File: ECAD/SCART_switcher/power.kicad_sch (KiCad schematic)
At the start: 18 parts, among them U12 L7805, U13 L7809, U14 TL431DBZ

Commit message: progressed ecad
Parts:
- removed U14: TL431DBZ, Package_TO_SOT_SMD:SOT-23, symbol Reference_Voltage:TL431DBZ
- added C?: 100nC, Capacitor_SMD:C_0805_2012Metric_Pad1.18x1.45mm_HandSolder, symbol Device:C
- added R? (x4): 10kR, Resistor_SMD:R_0805_2012Metric_Pad1.20x1.40mm_HandSolder, symbol Device:R
- added SW1: SW_Push_DPDT, symbol Switch:SW_Push_DPDT
- added U? (x3): RC4580, symbol Amplifier_Operational:NE5532
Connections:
- net +12V: now also C?.1, U?.8 (V+)
- net +2V5: now also U?.1, U?.2 (-)
- net +4V5: now also U?.6 (-), U?.7
- net +5V: now also R?.1
- net +9V: now also R?.1
- net GND: now also C?.2, R?.2, R?.2, U?.4 (V-)
- net at D?.2 (A2), Q?.5 (D), Q?.6 (D)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: now also SW1.3 (C), SW1.6 (C); no longer J?.1
- new net: J?.1, SW1.2 (B), SW1.5 (B)
- new net: R?.1, R?.2, U?.5 (+)
- new net: R?.1, R?.2, U?.3 (+)
- no-connect marks 0 -> 2
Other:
- moved on the sheet: C?, D?, FB?, J?, Q?, R?, U12, U13

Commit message: progressed ECAD.
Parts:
- removed U? (x3): RC4580, symbol Amplifier_Operational:NE5532
- added C32 (x2): 10uC, symbol Device:C
- added C? (x3): 100nC, Capacitor_SMD:C_0805_2012Metric_Pad1.18x1.45mm_HandSolder, symbol Device:C
- added R? (x4): 100R, Resistor_SMD:R_0805_2012Metric_Pad1.20x1.40mm_HandSolder, symbol Device:R
- added U? (x6): RC4580, symbol Amplifier_Operational:NE5532
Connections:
- net +12V: no longer C?.1
- net +2V5: now also C32.2, C?.1, R?.2, R?.2
- net +4V5: now also C?.1, C32.2, R?.2, R?.2
- net +5V: now also C?.1, U?.8 (V+)
- net +9V: now also C?.1, U?.8 (V+)
- net GND: now also C32.1, C32.1, C?.2, C?.2, C?.2, U?.4 (V-), U?.4 (V-)
- net at R?.1, R?.2: now also U?.3 (+), U?.5 (+) (x2)
- new net: R?.1, U?.6 (-), U?.7 (x2)
- new net: R?.1, U?.1, U?.2 (-) (x2)
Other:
- moved on the sheet: C?, D?, FB?, J?, Q?, R?, SW1, U12, U13

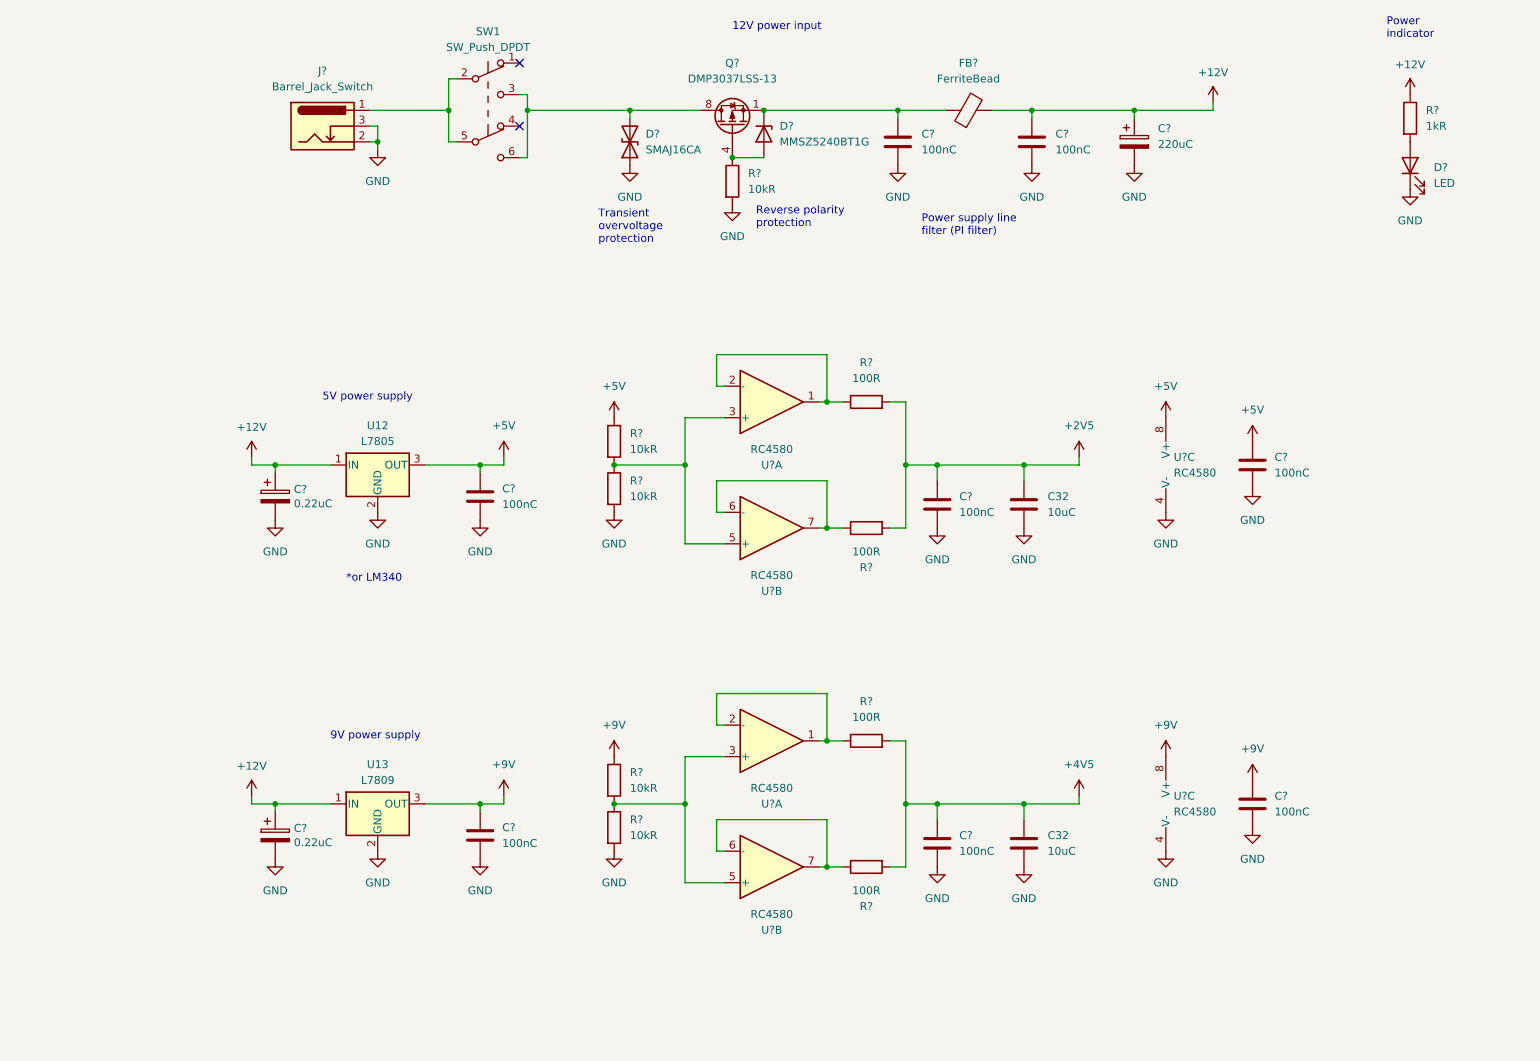
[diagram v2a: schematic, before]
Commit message: ERC fixes.
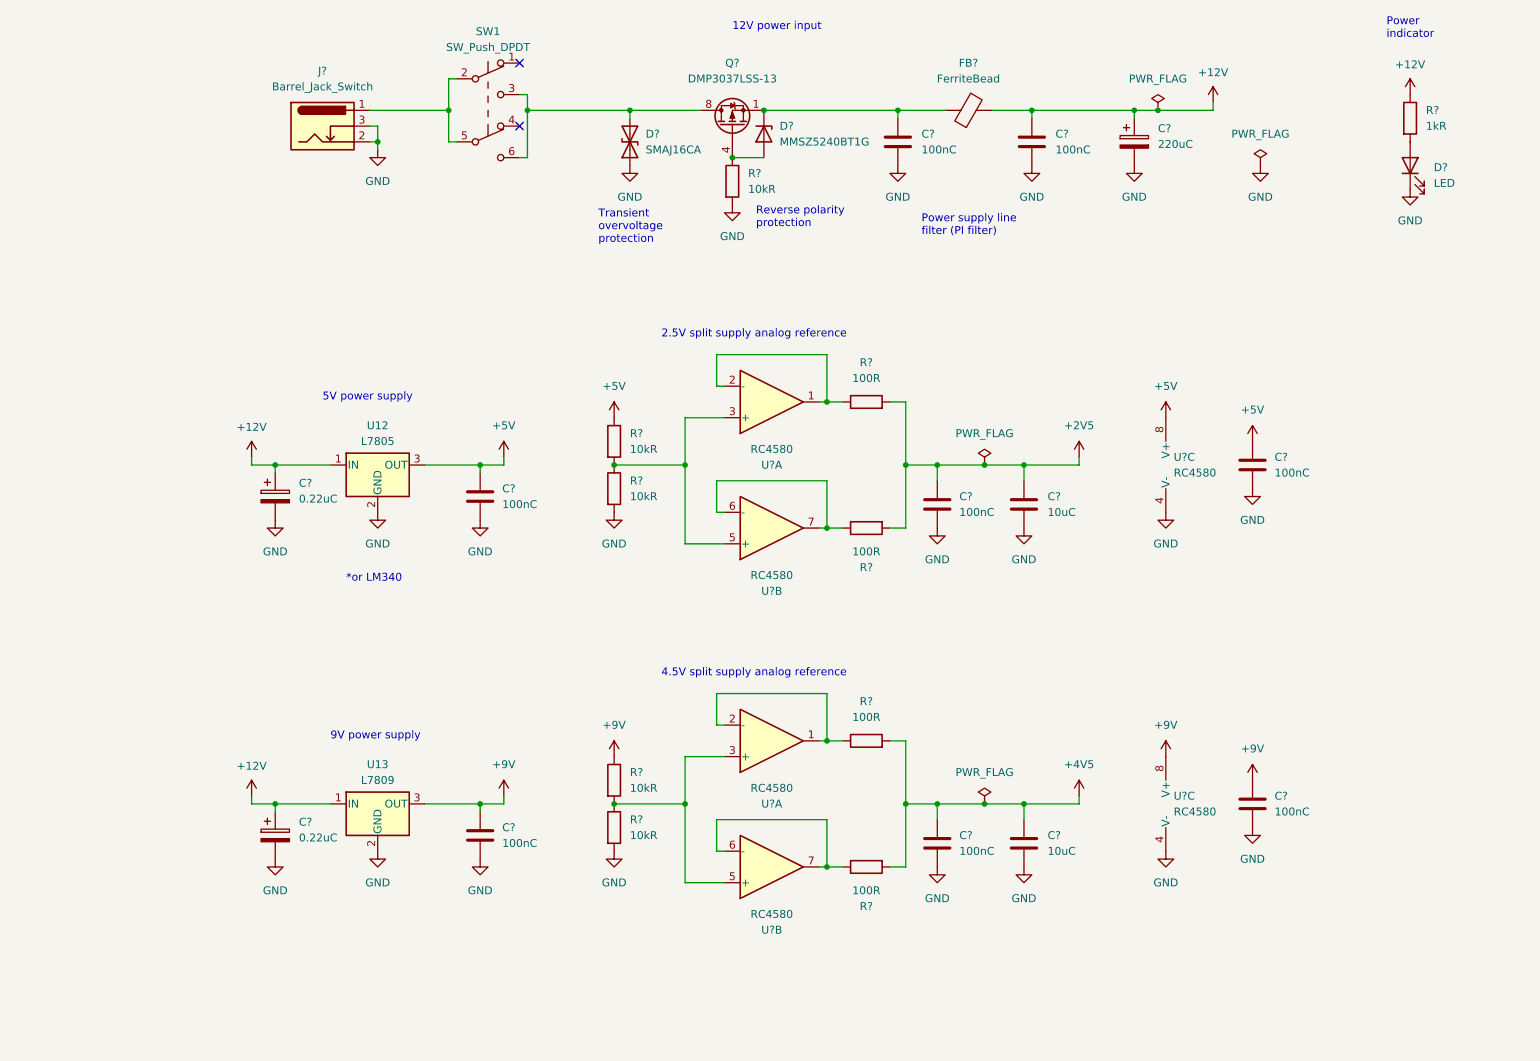
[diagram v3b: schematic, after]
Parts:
- removed C? (x2): 0.22uC, Capacitor_Tantalum_SMD:CP_EIA-3216-18_Kemet-A_Pad1.58x1.35mm_HandSolder, symbol LightSource-rescue:CP-Device
- added C? (x2): 0.22uC, Capacitor_Tantalum_SMD:CP_EIA-3216-18_Kemet-A_Pad1.58x1.35mm_HandSolder, symbol Device:C_Polarized
- renumbered C32 to C?
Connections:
- net +12V: now also C?.1, C?.1
- net GND: now also C?.2, C?.2
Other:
- note added: "2.5V split supply analog reference"
- note added: "4.5V split supply analog reference"

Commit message: progressed ecad
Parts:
- added C? (x2): 0.22uC, Capacitor_Tantalum_SMD:CP_EIA-3216-18_Kemet-A_Pad1.58x1.35mm_HandSolder, symbol Device:C_Polarized
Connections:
- net GND: now also C?.2, C?.2
- net at R?.1, R?.2, U?.3 (+)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: now also C?.1 (x2)
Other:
- moved on the sheet: C?, R?, U12, U13

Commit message: Progressed ECAD. Error fixing and cleanup.
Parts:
- removed D?: MMSZ5240BT1G, Diode_SMD:D_SOD-123, symbol Device:D_Zener
- added D22: BZX84C10, Package_TO_SOT_SMD:SOT-23, symbol Diode:BZX84Cxx
- renumbered U12 to U11, U13 to U12
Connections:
- net at C?.2, FB?.1, Q?.1 (S)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: now also D22.3 (K)
- net at Q?.4 (G), R?.1: now also D22.1 (A)
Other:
- note added: "0.3W min"

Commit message: Progressed ECAD.
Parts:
- R? (x4): MPN (none) -> RC0805FR-0710KL
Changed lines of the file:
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@@
       (effects (font (size 1.27 1.27)) hide)
     )
-    (property "MFN" "" (at 87.63 148.59 0)
-      (effects (font (size 1.27 1.27)) hide)
-    )
     (property "MPN" "CL21B104KBCNNNC" (at 87.63 148.59 0)
       (effects (font (size 1.27 1.27)) hide)
@@
       (effects (font (size 1.27 1.27)) hide)
     )
-    (property "Datasheet" "~" (at 109.22 148.59 0)
+    (property "Datasheet" "https://datasheet.lcsc.com/lcsc/1810201611_YAGEO-RC0805FR-0710KL_C84376.pdf" (at 109.22 148.59 0)
+      (effects (font (size 1.27 1.27)) hide)
+    )
+    (property "MPN" "RC0805FR-0710KL" (at 109.22 148.59 0)
       (effects (font (size 1.27 1.27)) hide)
     )
@@
       (effects (font (size 1.27 1.27)) hide)
     )
-    (property "MFN" "" (at 87.63 93.98 0)
-      (effects (font (size 1.27 1.27)) hide)
-    )
     (property "MPN" "CL21B104KBCNNNC" (at 87.63 93.98 0)
       (effects (font (size 1.27 1.27)) hide)
@@
       (effects (font (size 1.27 1.27)) hide)
     )
-    (property "Datasheet" "~" (at 109.22 83.82 0)
+    (property "Datasheet" "https://datasheet.lcsc.com/lcsc/1810201611_YAGEO-RC0805FR-0710KL_C84376.pdf" (at 109.22 83.82 0)
+      (effects (font (size 1.27 1.27)) hide)
+    )
+    (property "MPN" "RC0805FR-0710KL" (at 109.22 83.82 0)
       (effects (font (size 1.27 1.27)) hide)
     )
@@
       (effects (font (size 1.27 1.27)) hide)
     )
-    (property "MFN" "" (at 224.79 143.51 0)
-      (effects (font (size 1.27 1.27)) hide)
-    )
     (property "MPN" "CL21B104KBCNNNC" (at 224.79 143.51 0)
       (effects (font (size 1.27 1.27)) hide)
@@
       (effects (font (size 1.27 1.27)) hide)
     )
-    (property "Datasheet" "~" (at 109.22 93.98 0)
+    (property "Datasheet" "https://datasheet.lcsc.com/lcsc/1810201611_YAGEO-RC0805FR-0710KL_C84376.pdf" (at 109.22 93.98 0)
+      (effects (font (size 1.27 1.27)) hide)
+    )
+    (property "MPN" "RC0805FR-0710KL" (at 109.22 93.98 0)
       (effects (font (size 1.27 1.27)) hide)
     )
@@
       (effects (font (size 1.27 1.27)) hide)
     )
-    (property "MFN" "" (at 173.99 149.86 0)
-      (effects (font (size 1.27 1.27)) hide)
-    )
     (property "MPN" "CL21B104KBCNNNC" (at 173.99 149.86 0)
       (effects (font (size 1.27 1.27)) hide)
@@
       (effects (font (size 1.27 1.27)) hide)
     )
-    (property "Datasheet" "~" (at 109.22 138.43 0)
+    (property "Datasheet" "https://datasheet.lcsc.com/lcsc/1810201611_YAGEO-RC0805FR-0710KL_C84376.pdf" (at 109.22 138.43 0)
+      (effects (font (size 1.27 1.27)) hide)
+    )
+    (property "MPN" "RC0805FR-0710KL" (at 109.22 138.43 0)
       (effects (font (size 1.27 1.27)) hide)
     )
@@
       (effects (font (size 1.27 1.27)) hide)
     )
-    (property "MFN" "" (at 224.79 88.9 0)
-      (effects (font (size 1.27 1.27)) hide)
-    )
     (property "MPN" "CL21B104KBCNNNC" (at 224.79 88.9 0)
       (effects (font (size 1.27 1.27)) hide)
@@
       (effects (font (size 1.27 1.27)) hide)
     )
-    (property "MFN" "" (at 173.99 95.25 0)
-      (effects (font (size 1.27 1.27)) hide)
-    )

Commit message: Progressed ECAD.
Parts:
- C? (x8): footprint Capacitor_SMD:C_0805_2012Metric_Pad1.18x1.45mm_HandSolder -> Capacitor_SMD:C_0805_2012Metric
- D?: footprint Diode_SMD:D_0805_2012Metric_Pad1.15x1.40mm_HandSolder -> LED_THT:LED_D5.0mm; MPN 17-21SYGC/S530-E3/TR8 -> 333-2SURD/S530-A3
- R? (x9): footprint Resistor_SMD:R_0805_2012Metric_Pad1.20x1.40mm_HandSolder -> Resistor_SMD:R_0805_2012Metric
- R?: footprint Resistor_SMD:R_1210_3225Metric_Pad1.30x2.65mm_HandSolder -> Resistor_SMD:R_1210_3225Metric
- U11, U12: footprint (none) -> Package_TO_SOT_THT:TO-220-3_Horizontal_TabUp
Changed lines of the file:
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@@
       (effects (font (size 1.27 1.27)) (justify right))
     )
-    (property "Footprint" "Capacitor_SMD:C_0805_2012Metric_Pad1.18x1.45mm_HandSolder" (at 166.6748 33.02 0)
+    (property "Footprint" "Capacitor_SMD:C_0805_2012Metric" (at 166.6748 33.02 0)
       (effects (font (size 1.27 1.27)) hide)
     )
@@
       (effects (font (size 1.27 1.27)) (justify left))
     )
-    (property "Footprint" "Capacitor_SMD:C_0805_2012Metric_Pad1.18x1.45mm_HandSolder" (at 88.5952 152.4 0)
+    (property "Footprint" "Capacitor_SMD:C_0805_2012Metric" (at 88.5952 152.4 0)
       (effects (font (size 1.27 1.27)) hide)
     )
@@
       (effects (font (size 1.27 1.27)) (justify left))
     )
-    (property "Footprint" "Resistor_SMD:R_0805_2012Metric_Pad1.20x1.40mm_HandSolder" (at 107.442 148.59 90)
+    (property "Footprint" "Resistor_SMD:R_0805_2012Metric" (at 107.442 148.59 90)
       (effects (font (size 1.27 1.27)) hide)
     )
@@
       (effects (font (size 1.27 1.27)))
     )
-    (property "Footprint" "Resistor_SMD:R_0805_2012Metric_Pad1.20x1.40mm_HandSolder" (at 162.56 151.892 90)
+    (property "Footprint" "Resistor_SMD:R_0805_2012Metric" (at 162.56 151.892 90)
       (effects (font (size 1.27 1.27)) hide)
     )
@@
       (effects (font (size 1.27 1.27)) (justify left))
     )
-    (property "Footprint" "Capacitor_SMD:C_0805_2012Metric_Pad1.18x1.45mm_HandSolder" (at 88.5952 97.79 0)
+    (property "Footprint" "Capacitor_SMD:C_0805_2012Metric" (at 88.5952 97.79 0)
       (effects (font (size 1.27 1.27)) hide)
     )
@@
       (effects (font (size 1.27 1.27)) (justify left))
     )
-    (property "Footprint" "Resistor_SMD:R_0805_2012Metric_Pad1.20x1.40mm_HandSolder" (at 107.442 83.82 90)
+    (property "Footprint" "Resistor_SMD:R_0805_2012Metric" (at 107.442 83.82 90)
       (effects (font (size 1.27 1.27)) hide)
     )
@@
       (effects (font (size 1.27 1.27)) (justify left))
     )
-    (property "Footprint" "Capacitor_SMD:C_0805_2012Metric_Pad1.18x1.45mm_HandSolder" (at 225.7552 147.32 0)
+    (property "Footprint" "Capacitor_SMD:C_0805_2012Metric" (at 225.7552 147.32 0)
       (effects (font (size 1.27 1.27)) hide)
     )
@@
       (effects (font (size 1.27 1.27)))
     )
-    (property "Footprint" "Resistor_SMD:R_0805_2012Metric_Pad1.20x1.40mm_HandSolder" (at 162.56 135.128 90)
+    (property "Footprint" "Resistor_SMD:R_0805_2012Metric" (at 162.56 135.128 90)
       (effects (font (size 1.27 1.27)) hide)
     )
@@
       (effects (font (size 1.27 1.27)) (justify left))
     )
-    (property "Footprint" "Resistor_SMD:R_0805_2012Metric_Pad1.20x1.40mm_HandSolder" (at 107.442 93.98 90)
+    (property "Footprint" "Resistor_SMD:R_0805_2012Metric" (at 107.442 93.98 90)
       (effects (font (size 1.27 1.27)) hide)
     )
@@
       (effects (font (size 1.27 1.27)) (justify left))
     )
-    (property "Footprint" "Resistor_SMD:R_1210_3225Metric_Pad1.30x2.65mm_HandSolder" (at 248.412 33.02 90)
+    (property "Footprint" "Resistor_SMD:R_1210_3225Metric" (at 248.412 33.02 90)
       (effects (font (size 1.27 1.27)) hide)
     )
@@
       (effects (font (size 1.27 1.27)) (justify left))
     )
-    (property "Footprint" "Capacitor_SMD:C_0805_2012Metric_Pad1.18x1.45mm_HandSolder" (at 174.9552 153.67 0)
+    (property "Footprint" "Capacitor_SMD:C_0805_2012Metric" (at 174.9552 153.67 0)
       (effects (font (size 1.27 1.27)) hide)
     )
@@
       (effects (font (size 1.27 1.27)))
     )
-    (property "Footprint" "Resistor_SMD:R_0805_2012Metric_Pad1.20x1.40mm_HandSolder" (at 162.56 80.518 90)
+    (property "Footprint" "Resistor_SMD:R_0805_2012Metric" (at 162.56 80.518 90)
       (effects (font (size 1.27 1.27)) hide)
     )
@@
       (effects (font (size 1.27 1.27)))
     )
-    (property "Footprint" "Resistor_SMD:R_0805_2012Metric_Pad1.20x1.40mm_HandSolder" (at 162.56 97.282 90)
+    (property "Footprint" "Resistor_SMD:R_0805_2012Metric" (at 162.56 97.282 90)
       (effects (font (size 1.27 1.27)) hide)
     )
@@
       (effects (font (size 1.27 1.27)))
     )
-    (property "Footprint" "" (at 71.755 92.71 0)
+    (property "Footprint" "Package_TO_SOT_THT:TO-220-3_Horizontal_TabUp" (at 71.755 92.71 0)
       (effects (font (size 1.27 1.27) italic) (justify left) hide)
     )
@@
       (effects (font (size 1.27 1.27)) (justify left))
     )
-    (property "Footprint" "Resistor_SMD:R_0805_2012Metric_Pad1.20x1.40mm_HandSolder" (at 107.442 138.43 90)
+    (property "Footprint" "Resistor_SMD:R_0805_2012Metric" (at 107.442 138.43 90)
       (effects (font (size 1.27 1.27)) hide)
     )
@@
       (effects (font (size 1.27 1.27)) (justify left))
     )
-    (property "Footprint" "Capacitor_SMD:C_0805_2012Metric_Pad1.18x1.45mm_HandSolder" (at 225.7552 92.71 0)
+    (property "Footprint" "Capacitor_SMD:C_0805_2012Metric" (at 225.7552 92.71 0)
       (effects (font (size 1.27 1.27)) hide)
     )
@@
       (effects (font (size 1.27 1.27)) (justify right))
     )
-    (property "Footprint" "Diode_SMD:D_0805_2012Metric_Pad1.15x1.40mm_HandSolder" (at 250.19 40.64 0)
+    (property "Footprint" "LED_THT:LED_D5.0mm" (at 250.19 40.64 0)
       (effects (font (size 1.27 1.27)) hide)
     )
-    (property "Datasheet" "https://datasheet.lcsc.com/lcsc/1810271707_Everlight-Elec-17-21SYGC-S530-E3-TR8_C142303.pdf" (at 250.19 40.64 0)
+    (property "Datasheet" "https://datasheet.lcsc.com/lcsc/1810271709_Everlight-Elec-333-2SURD-S530-A3_C87271.pdf" (at 250.19 40.64 0)
       (effects (font (size 1.27 1.27)) hide)
     )
-    (property "MPN" "17-21SYGC/S530-E3/TR8" (at 250.19 40.64 0)
+    (property "MPN" "333-2SURD/S530-A3" (at 250.19 40.64 0)
       (effects (font (size 1.27 1.27)) hide)
     )
@@
       (effects (font (size 1.27 1.27)) (justify right))
     )
-    (property "Footprint" "Capacitor_SMD:C_0805_2012Metric_Pad1.18x1.45mm_HandSolder" (at 188.2648 33.02 0)
+    (property "Footprint" "Capacitor_SMD:C_0805_2012Metric" (at 188.2648 33.02 0)
       (effects (font (size 1.27 1.27)) hide)
     )
@@
       (effects (font (size 1.27 1.27)) (justify left))
     )
-    (property "Footprint" "Capacitor_SMD:C_0805_2012Metric_Pad1.18x1.45mm_HandSolder" (at 174.9552 99.06 0)
+    (property "Footprint" "Capacitor_SMD:C_0805_2012Metric" (at 174.9552 99.06 0)
       (effects (font (size 1.27 1.27)) hide)
     )
@@
       (effects (font (size 1.27 1.27)))
     )
-    (property "Footprint" "" (at 71.755 147.32 0)
+    (property "Footprint" "Package_TO_SOT_THT:TO-220-3_Horizontal_TabUp" (at 71.755 147.32 0)
       (effects (font (size 1.27 1.27) italic) (justify left) hide)
     )
@@
       (effects (font (size 1.27 1.27)) (justify left))
     )
-    (property "Footprint" "Resistor_SMD:R_0805_2012Metric_Pad1.20x1.40mm_HandSolder" (at 139.192 43.18 90)
+    (property "Footprint" "Resistor_SMD:R_0805_2012Metric" (at 139.192 43.18 90)
       (effects (font (size 1.27 1.27)) hide)
     )
